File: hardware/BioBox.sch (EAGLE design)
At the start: 12 parts, among them IC1 MCP23017SP

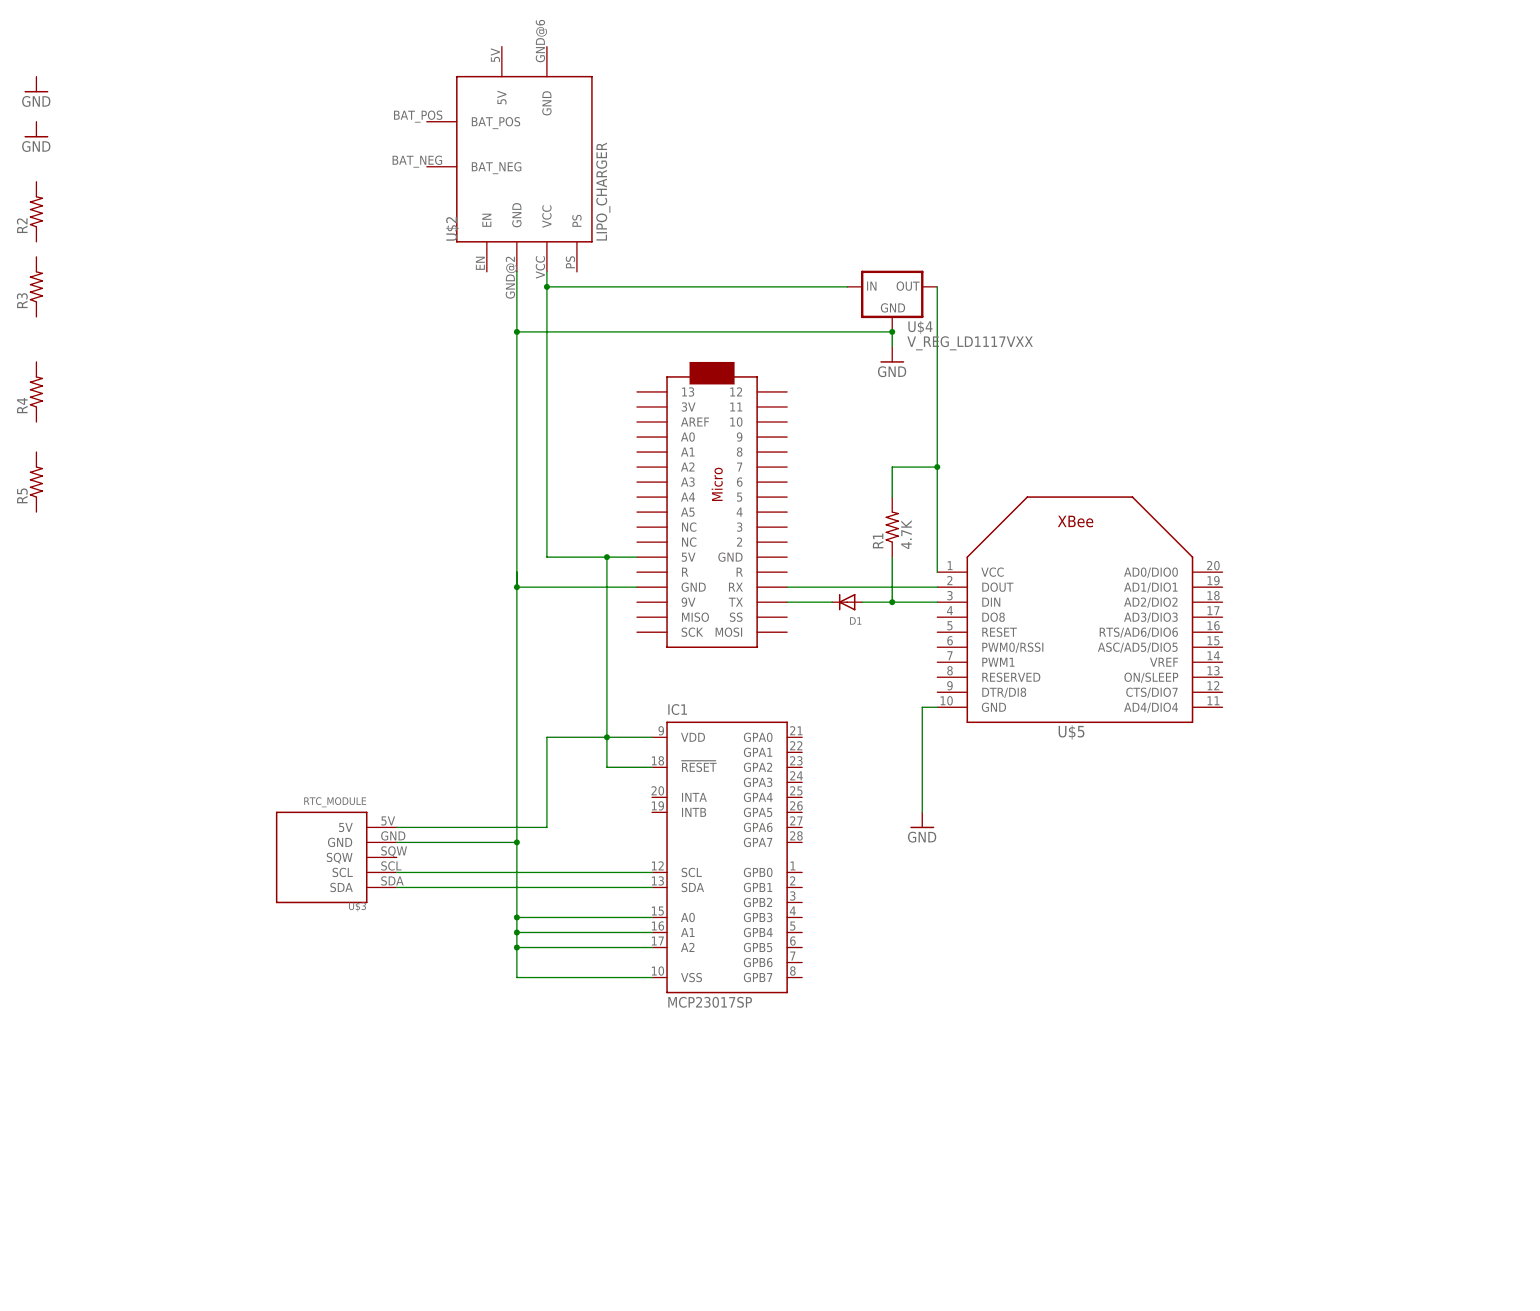
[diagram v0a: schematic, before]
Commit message: finished first pass of schematic
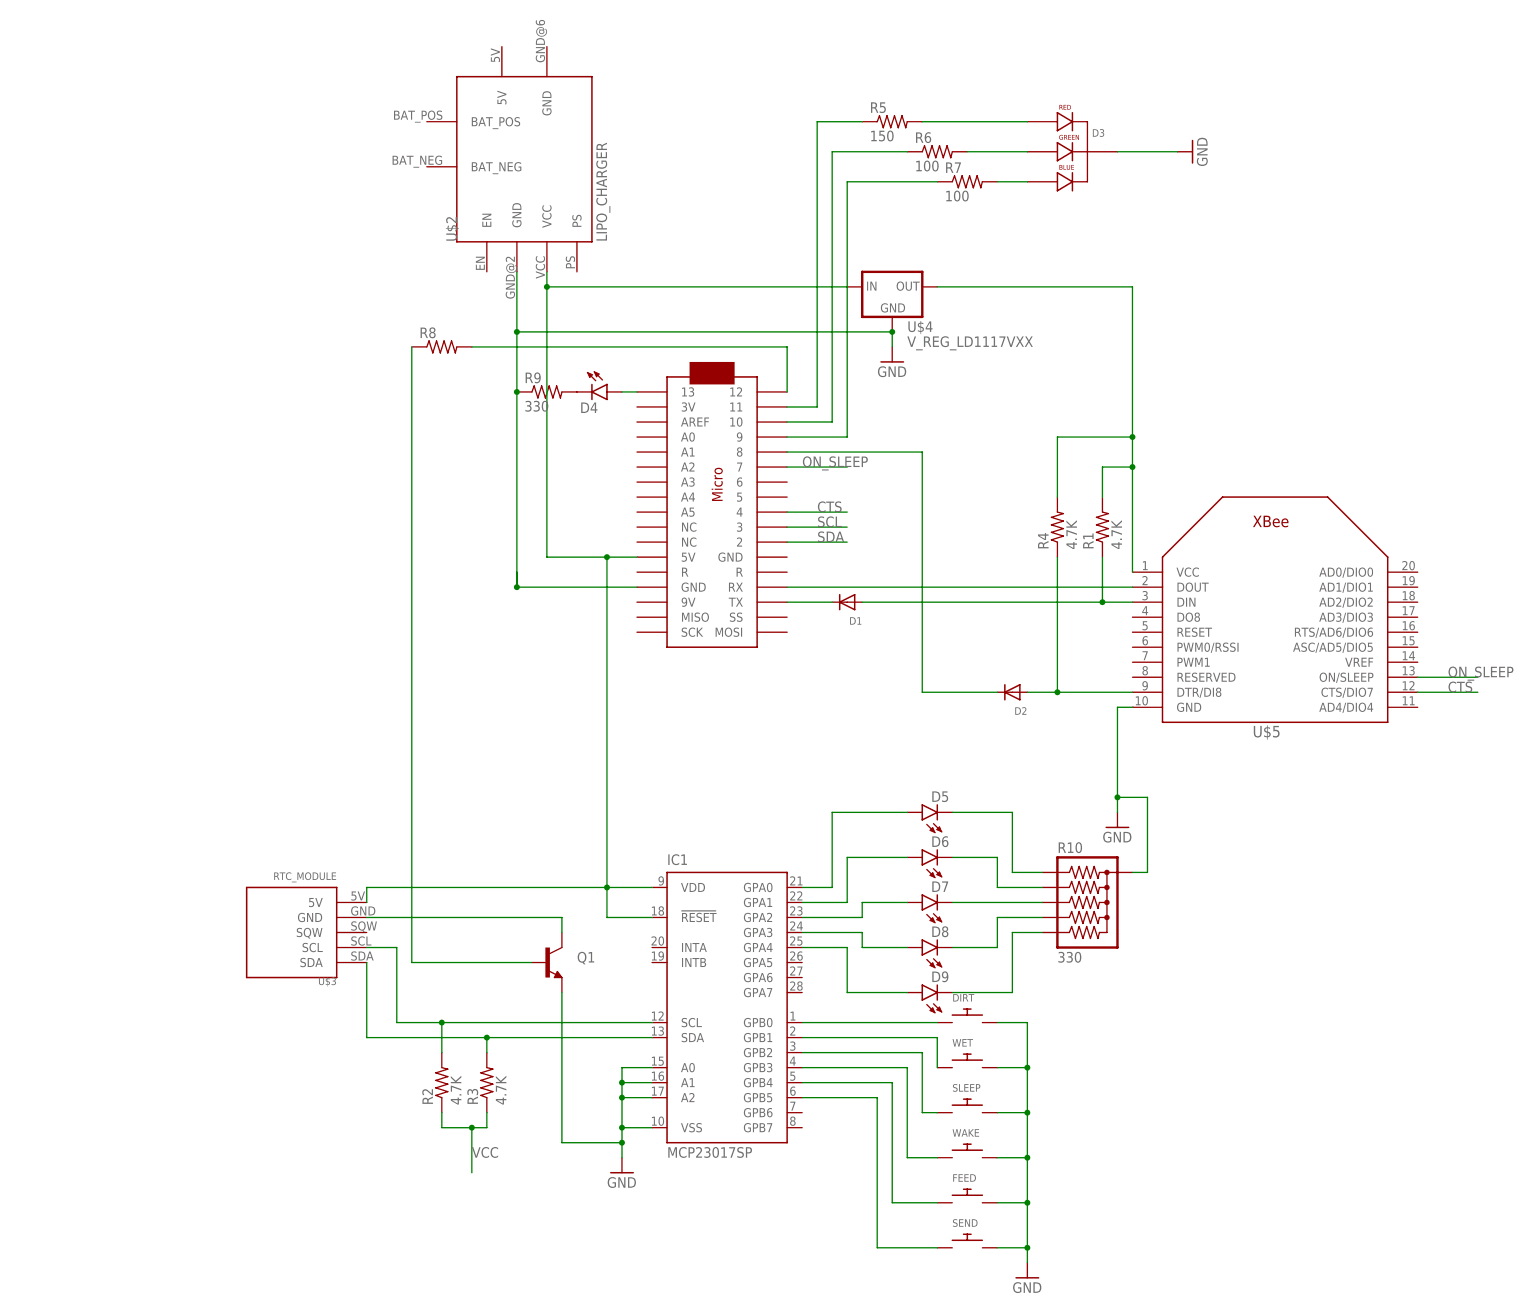
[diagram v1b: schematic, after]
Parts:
- added D2: (no value), adafruit:DIODEDO-1N4148
- added D3: LED-RGB-CC-THRUDIFFUSE, SparkFun-LED:LED-RGB-CC-THRUDIFFUSE
- added D4, D5, D6, D7, D8, D9: (no value), SparkFun-LED:LED5MM
- added DIRT, FEED, SEND, SLEEP, WAKE, WET: (no value), adafruit:SWITCH_PUSHBUTTONSOFTTOUCHSMD_SJ
- added Q1: (no value), SparkFun-DiscreteSemi:TRANSISTOR_NPN2N3904
- added R10: 330, SparkFun-Passives:RPACK-BUSSED-SIP-PTH-5
- added R6, R7: 100, SparkFun-Passives:RESISTORPTH-1/4W
- added R8: (no value), SparkFun-Passives:RESISTORPTH-1/4W
- added R9: 330, SparkFun-Passives:RESISTORPTH-1/4W
- R2, R3, R4: value (none) -> 4.7K
- R5: value (none) -> 150
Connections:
- new net CTS: U$1.4, U$5.CTS/DIO7
- new net N$10: D3.RED_CATHODE, R5.2
- new net N$11: D3.GREEN_CATHODE, R6.2
- new net N$12: D3.BLUE_CATHODE, R7.2
- new net N$13: DIRT.P$1, IC1.GPB0
- new net N$14: IC1.GPB1, WET.P$1
- new net N$15: IC1.GPB2, SLEEP.P$1
- new net N$16: IC1.GPB3, WAKE.P$1
- new net N$17: FEED.P$1, IC1.GPB4
- new net N$18: IC1.GPB5, SEND.P$1
- new net N$19: Q1.C, U$3.GND
- new net N$20: R8.2, U$1.12
- new net N$21: D4.C, R9.2
- new net N$22: Q1.B, R8.1
- new net N$23: D4.A, U$1.13
- new net N$24: D5.A, IC1.GPA0
- new net N$25: D6.A, IC1.GPA1
- new net N$26: D7.A, IC1.GPA2
- new net N$27: D8.A, IC1.GPA3
- new net N$28: D9.A, IC1.GPA4
- new net N$29: D5.C, R10.2
- new net N$30: D6.C, R10.3
- new net N$31: D7.C, R10.4
- new net N$32: D8.C, R10.5
- new net N$33: D9.C, R10.6
- new net N$7: R7.1, U$1.9
- new net N$8: R6.1, U$1.10
- new net N$9: R5.1, U$1.11
- new net ON_SLEEP: U$1.7, U$5.ON/SLEEP
- new net SCL: IC1.SCL, R2.2, U$1.3, U$3.SCL
- new net SDA: IC1.SDA, R3.2, U$1.2, U$3.SDA
- net GND: now also D3.CATHODE, DIRT.P$2, FEED.P$2, Q1.E, R10.1, R9.1, SEND.P$2, SLEEP.P$2, WAKE.P$2, WET.P$2; no longer U$3.GND
- net N$1: now also D2.A, R4.1, U$5.DTR/DI8; no longer IC1.SCL, U$3.SCL
- net N$2: now also D2.C, U$1.8; no longer IC1.SDA, U$3.SDA
- net VCC: now also R2.1, R3.1, R4.2
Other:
- moved on the sheet: IC1, R1, R2, R3, R4, R5, U$3, U$5

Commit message: Changes to schematic to reflect modifications made when breadboarding circuit
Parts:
- removed Q1: (no value), SparkFun-DiscreteSemi:TRANSISTOR_NPN2N3904
- removed R8: (no value), SparkFun-Passives:RESISTORPTH-1/4W
- added C1: (no value), SparkFun-Passives:CAPPTH
- added C2: (no value), SparkFun-Passives:CAP_POLPTH1
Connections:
- removed net N$19: Q1.C, U$3.GND
- removed net N$20: R8.2, U$1.12
- removed net N$22: Q1.B, R8.1
- net GND: now also C1.2, C2.-; no longer Q1.E
- net N$4: now also C1.1
- net ON_SLEEP: now also U$1.6; no longer U$1.7
- net VCC: now also C2.+
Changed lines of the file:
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@@
 <part name="R6" library="SparkFun-Passives" deviceset="RESISTOR" device="PTH-1/4W" value="100"/>
 <part name="R7" library="SparkFun-Passives" deviceset="RESISTOR" device="PTH-1/4W" value="100"/>
-<part name="R8" library="SparkFun-Passives" deviceset="RESISTOR" device="PTH-1/4W"/>
 <part name="DIRT" library="adafruit" deviceset="SWITCH_PUSHBUTTON" device="SOFTTOUCHSMD_SJ"/>
 <part name="WET" library="adafruit" deviceset="SWITCH_PUSHBUTTON" device="SOFTTOUCHSMD_SJ"/>
@@
 <part name="SEND" library="adafruit" deviceset="SWITCH_PUSHBUTTON" device="SOFTTOUCHSMD_SJ"/>
 <part name="GND5" library="SparkFun-Aesthetics" deviceset="GND" device=""/>
-<part name="Q1" library="SparkFun-DiscreteSemi" deviceset="TRANSISTOR_NPN" device="2N3904"/>
 <part name="R9" library="SparkFun-Passives" deviceset="RESISTOR" device="PTH-1/4W" value="330"/>
 <part name="R10" library="SparkFun-Passives" deviceset="RPACK*" device="-BUSSED-SIP-PTH-5" value="330"/>
@@
 <part name="D8" library="SparkFun-LED" deviceset="LED" device="5MM"/>
 <part name="D9" library="SparkFun-LED" deviceset="LED" device="5MM"/>
+<part name="C1" library="SparkFun-Passives" deviceset="CAP" device="PTH"/>
+<part name="C2" library="SparkFun-Passives" deviceset="CAP_POL" device="PTH1"/>
 </parts>
 <sheets>
@@
 <instance part="R6" gate="G$1" x="119.38" y="142.24"/>
 <instance part="R7" gate="G$1" x="124.46" y="137.16"/>
-<instance part="R8" gate="G$1" x="35.56" y="109.22"/>
 <instance part="DIRT" gate="G$1" x="124.46" y="-5.08"/>
 <instance part="WET" gate="G$1" x="124.46" y="-12.7"/>
@@
 <instance part="SEND" gate="G$1" x="124.46" y="-43.18"/>
 <instance part="GND5" gate="1" x="134.62" y="-48.26"/>
-<instance part="Q1" gate="G$1" x="53.34" y="5.08"/>
 <instance part="R9" gate="G$1" x="53.34" y="101.6"/>
 <instance part="R10" gate="G$1" x="137.16" y="20.32"/>
@@
 <instance part="D8" gate="G$1" x="116.84" y="7.62" rot="R90"/>
 <instance part="D9" gate="G$1" x="116.84" y="0" rot="R90"/>
+<instance part="C1" gate="G$1" x="88.9" y="114.3"/>
+<instance part="C2" gate="G$1" x="124.46" y="116.84"/>
 </instances>
 <busses>
@@
 <wire x1="63.5" y1="12.7" x2="63.5" y2="17.78" width="0.1524" layer="91"/>
 <pinref part="U$4" gate="G$1" pin="IN"/>
-<wire x1="104.14" y1="119.38" x2="53.34" y2="119.38" width="0.1524" layer="91"/>
+<wire x1="104.14" y1="119.38" x2="88.9" y2="119.38" width="0.1524" layer="91"/>
 <junction x="53.34" y="119.38"/>
 <pinref part="U$3" gate="G$1" pin="5V"/>
+<wire x1="88.9" y1="119.38" x2="53.34" y2="119.38" width="0.1524" layer="91"/>
 <wire x1="63.5" y1="17.78" x2="22.86" y2="17.78" width="0.1524" layer="91"/>
 <wire x1="22.86" y1="17.78" x2="22.86" y2="15.24" width="0.1524" layer="91"/>
+<pinref part="C1" gate="G$1" pin="1"/>
+<junction x="88.9" y="119.38"/>
 </segment>
 </net>
@@
 <wire x1="147.32" y1="88.9" x2="147.32" y2="83.82" width="0.1524" layer="91"/>
 <pinref part="U$4" gate="G$1" pin="OUT"/>
-<wire x1="119.38" y1="119.38" x2="152.4" y2="119.38" width="0.1524" layer="91"/>
+<wire x1="119.38" y1="119.38" x2="124.46" y2="119.38" width="0.1524" layer="91"/>
+<wire x1="124.46" y1="119.38" x2="152.4" y2="119.38" width="0.1524" layer="91"/>
 <wire x1="152.4" y1="119.38" x2="152.4" y2="93.98" width="0.1524" layer="91"/>
 <junction x="152.4" y="88.9"/>
@@
 <wire x1="139.7" y1="93.98" x2="139.7" y2="83.82" width="0.1524" layer="91"/>
 <junction x="152.4" y="93.98"/>
+<pinref part="C2" gate="G$1" pin="+"/>
+<junction x="124.46" y="119.38"/>
 </segment>
 <segment>
@@
 <junction x="48.26" y="68.58"/>
 <pinref part="U$4" gate="G$1" pin="GND"/>
-<wire x1="111.76" y1="111.76" x2="48.26" y2="111.76" width="0.1524" layer="91"/>
+<wire x1="111.76" y1="111.76" x2="88.9" y2="111.76" width="0.1524" layer="91"/>
 <junction x="48.26" y="111.76"/>
 <pinref part="GND2" gate="1" pin="GND"/>
+<wire x1="88.9" y1="111.76" x2="48.26" y2="111.76" width="0.1524" layer="91"/>
 <wire x1="111.76" y1="109.22" x2="111.76" y2="111.76" width="0.1524" layer="91"/>
 <junction x="111.76" y="111.76"/>
 <pinref part="R9" gate="G$1" pin="1"/>
 <junction x="48.26" y="101.6"/>
+<pinref part="C1" gate="G$1" pin="2"/>
+<junction x="88.9" y="111.76"/>
+<pinref part="C2" gate="G$1" pin="-"/>
+<wire x1="111.76" y1="111.76" x2="124.46" y2="111.76" width="0.1524" layer="91"/>
 </segment>
 <segment>
@@
 <pinref part="GND4" gate="1" pin="GND"/>
 <wire x1="71.12" y1="-22.86" x2="66.04" y2="-22.86" width="0.1524" layer="91"/>
-<wire x1="66.04" y1="-22.86" x2="66.04" y2="-25.4" width="0.1524" layer="91"/>
 <pinref part="IC1" gate="G$1" pin="A2"/>
-<wire x1="66.04" y1="-25.4" x2="66.04" y2="-27.94" width="0.1524" layer="91"/>
+<wire x1="66.04" y1="-22.86" x2="66.04" y2="-27.94" width="0.1524" layer="91"/>
 <wire x1="71.12" y1="-17.78" x2="66.04" y2="-17.78" width="0.1524" layer="91"/>
 <wire x1="66.04" y1="-17.78" x2="66.04" y2="-22.86" width="0.1524" layer="91"/>
@@
 <wire x1="66.04" y1="-12.7" x2="66.04" y2="-15.24" width="0.1524" layer="91"/>
 <junction x="66.04" y="-15.24"/>
-<pinref part="Q1" gate="G$1" pin="E"/>
-<wire x1="55.88" y1="0" x2="55.88" y2="-25.4" width="0.1524" layer="91"/>
-<wire x1="55.88" y1="-25.4" x2="66.04" y2="-25.4" width="0.1524" layer="91"/>
-<junction x="66.04" y="-25.4"/>
 </segment>
 <segment>
@@
 <net name="ON_SLEEP" class="0">
 <segment>
-<pinref part="U$1" gate="G$1" pin="7"/>
-<wire x1="93.98" y1="88.9" x2="104.14" y2="88.9" width="0.1524" layer="91"/>
-<label x="96.52" y="88.9" size="1.778" layer="95"/>
-</segment>
-<segment>
 <pinref part="U$5" gate="G$1" pin="ON/SLEEP"/>
 <wire x1="200.66" y1="53.34" x2="210.82" y2="53.34" width="0.1524" layer="91"/>
 <label x="205.74" y="53.34" size="1.778" layer="95"/>
+</segment>
+<segment>
+<pinref part="U$1" gate="G$1" pin="6"/>
+<wire x1="93.98" y1="86.36" x2="104.14" y2="86.36" width="0.1524" layer="91"/>
+<label x="96.52" y="86.36" size="1.778" layer="95"/>
 </segment>
 </net>
@@
 </segment>
 </net>
-<net name="N$22" class="0">
-<segment>
-<pinref part="R8" gate="G$1" pin="1"/>
-<wire x1="30.48" y1="109.22" x2="30.48" y2="5.08" width="0.1524" layer="91"/>
-<pinref part="Q1" gate="G$1" pin="B"/>
-<wire x1="50.8" y1="5.08" x2="30.48" y2="5.08" width="0.1524" layer="91"/>
-</segment>
-</net>
-<net name="N$19" class="0">
-<segment>
-<pinref part="U$3" gate="G$1" pin="GND"/>
-<pinref part="Q1" gate="G$1" pin="C"/>
-<wire x1="22.86" y1="12.7" x2="55.88" y2="12.7" width="0.1524" layer="91"/>
-<wire x1="55.88" y1="12.7" x2="55.88" y2="10.16" width="0.1524" layer="91"/>
-</segment>
-</net>
-<net name="N$20" class="0">
-<segment>
-<pinref part="R8" gate="G$1" pin="2"/>
-<wire x1="40.64" y1="109.22" x2="93.98" y2="109.22" width="0.1524" layer="91"/>
-<pinref part="U$1" gate="G$1" pin="12"/>
-<wire x1="93.98" y1="109.22" x2="93.98" y2="101.6" width="0.1524" layer="91"/>
-</segment>
-</net>
